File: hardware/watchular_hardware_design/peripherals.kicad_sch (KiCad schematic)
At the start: 45 parts, among them Q1 BSS123, Q2 BSS123, Q3 BSS123, Q4 BSS123

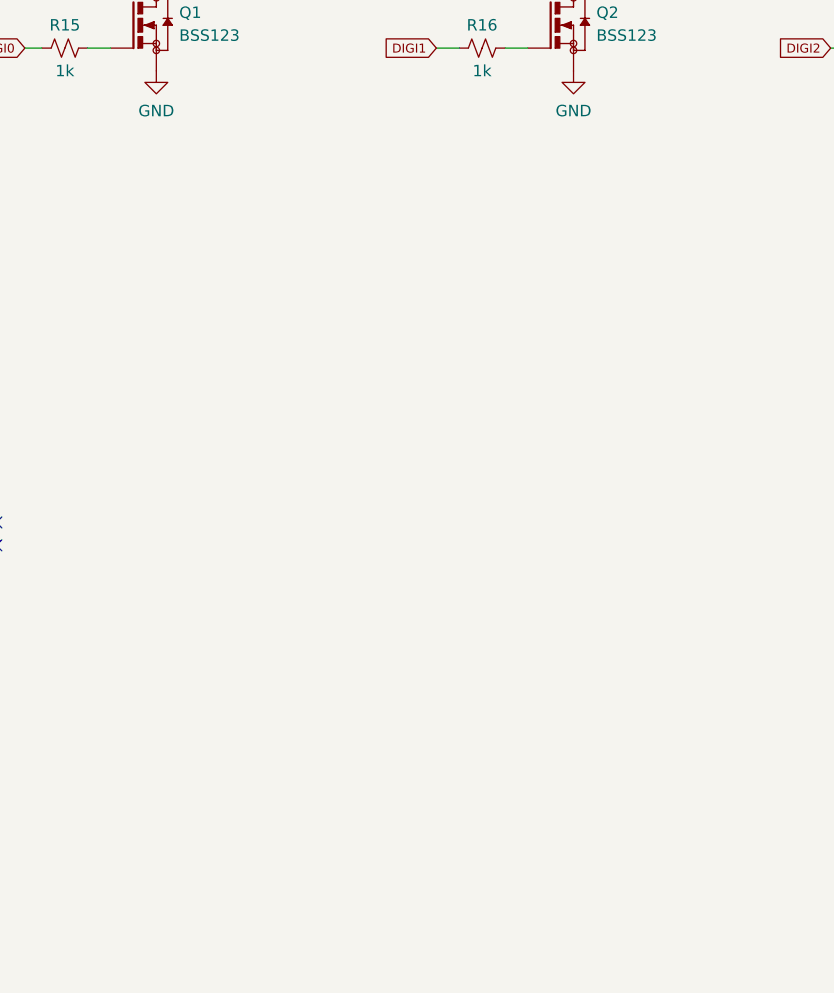
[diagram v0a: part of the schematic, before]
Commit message: Connected MCU pins to the brekout 15 pos header.
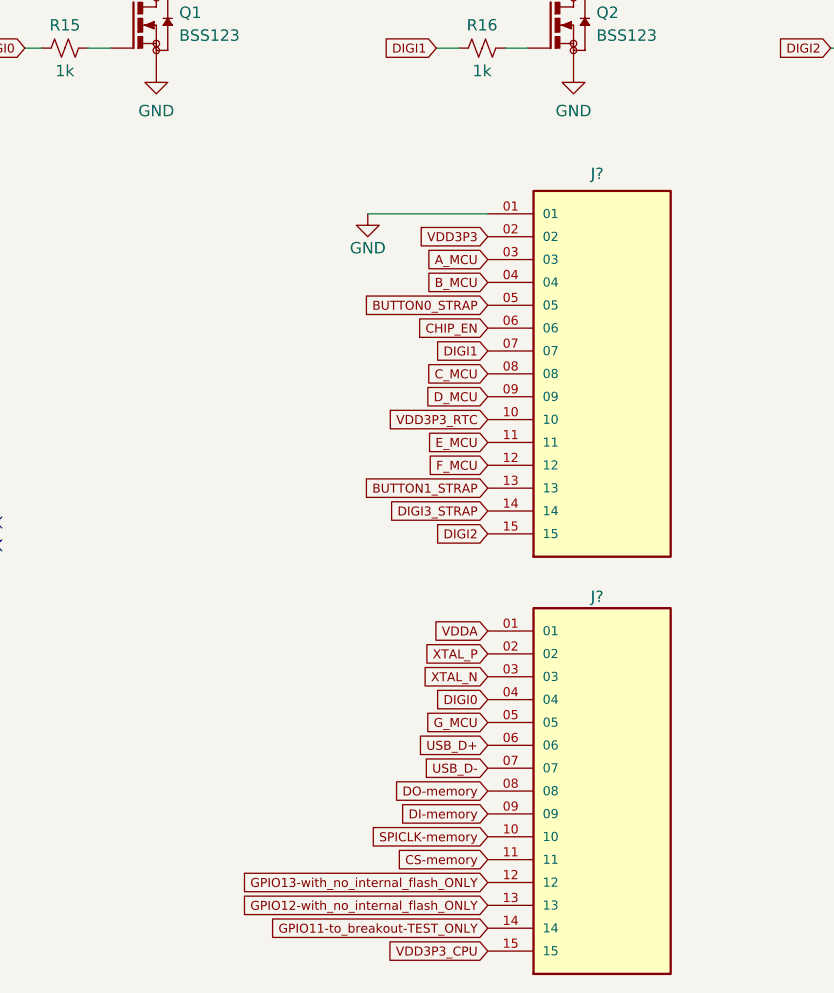
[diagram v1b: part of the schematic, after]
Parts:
- added J? (x2): TSW-115-07-H-S, SAMTEC_TSW-115-07-H-S, symbol TSW-115-07-H-S:TSW-115-07-H-S
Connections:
- net A_MCU: now also J?.03
- net BUTTON0_STRAP: now also J?.05
- net BUTTON1_STRAP: now also J?.13
- net B_MCU: now also J?.04
- net C_MCU: now also J?.08
- net DIGI0: now also J?.04
- net DIGI1: now also J?.07
- net DIGI2: now also J?.15
- net DIGI3_STRAP: now also J?.14
- net D_MCU: now also J?.09
- net E_MCU: now also J?.11
- net F_MCU: now also J?.12
- net GND: now also J?.01
- net G_MCU: now also J?.05
- new net CHIP_EN: J?.06
- new net CS-memory: J?.11
- new net DI-memory: J?.09
- new net DO-memory: J?.08
- new net GPIO11-to_breakout-TEST_ONLY: J?.14
- new net GPIO12-with_no_internal_flash_ONLY: J?.13
- new net GPIO13-with_no_internal_flash_ONLY: J?.12
- new net SPICLK-memory: J?.10
- new net USB_D+: J?.06
- new net USB_D-: J?.07
- new net VDD3P3: J?.02
- new net VDD3P3_CPU: J?.15
- new net VDD3P3_RTC: J?.10
- new net VDDA: J?.01
- new net XTAL_N: J?.03
- new net XTAL_P: J?.02

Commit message: Added battery connector.
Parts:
- added J4: 665102131822, battery_connector-665102131822:665102131822, symbol 665102131822:665102131822
- gave numbers to parts that had none: 2
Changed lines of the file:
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@@
   (symbol (lib_id "power:GND") (at 136.525 88.265 0) (unit 1)
     (in_bom yes) (on_board yes) (fields_autoplaced)
-    (property "Reference" "#PWR032" (id 0) (at 136.525 94.615 0)
+    (property "Reference" "#PWR033" (id 0) (at 136.525 94.615 0)
       (effects (font (size 1.27 1.27)) hide)
     )
@@
   (symbol (lib_id "power:GND") (at 180.34 88.265 0) (unit 1)
     (in_bom yes) (on_board yes) (fields_autoplaced)
-    (property "Reference" "#PWR033" (id 0) (at 180.34 94.615 0)
+    (property "Reference" "#PWR034" (id 0) (at 180.34 94.615 0)
       (effects (font (size 1.27 1.27)) hide)
     )
@@
   (symbol (lib_id "TSW-115-07-H-S:TSW-115-07-H-S") (at 139.7 168.275 0) (unit 1)
     (in_bom yes) (on_board yes)
-    (property "Reference" "J?" (id 0) (at 138.43 146.685 0)
+    (property "Reference" "J3" (id 0) (at 138.43 146.685 0)
       (effects (font (size 1.27 1.27)) (justify left))
     )
@@
   (symbol (lib_id "TSW-115-07-H-S:TSW-115-07-H-S") (at 139.7 121.92 0) (unit 1)
     (in_bom yes) (on_board yes)
-    (property "Reference" "J?" (id 0) (at 138.43 99.695 0)
+    (property "Reference" "J2" (id 0) (at 138.43 99.695 0)
       (effects (font (size 1.27 1.27)) (justify left))
     )
@@
   (symbol (lib_id "power:GND") (at 113.665 104.14 0) (unit 1)
     (in_bom yes) (on_board yes)
-    (property "Reference" "#PWR?" (id 0) (at 113.665 110.49 0)
+    (property "Reference" "#PWR032" (id 0) (at 113.665 110.49 0)
       (effects (font (size 1.27 1.27)) hide)
     )
@@
     (pin "2")
   )
+  (symbol (lib_id "665102131822:665102131822") (at 193.04 121.92 0) (unit 1)
+    (in_bom yes) (on_board yes) (fields_autoplaced)
+    (property "Reference" "J4" (id 0) (at 204.47 121.9199 0)
+      (effects (font (size 1.27 1.27)) (justify left))
+    )
+    (property "Value" "665102131822" (id 1) (at 204.47 124.4599 0)
+      (effects (font (size 1.27 1.27)) (justify left))
+    )
+    (property "Footprint" "battery_connector-665102131822:665102131822" (id 2) (at 193.04 121.92 0)
+      (effects (font (size 1.27 1.27)) (justify left bottom) hide)
+    )
+    (property "Datasheet" "" (id 3) (at 193.04 121.92 0)
+      (effects (font (size 1.27 1.27)) (justify left bottom) hide)
+    )
+    (pin "1")
+    (pin "2")
+  )
   (symbol (lib_id "TL3301AF260QG:TL3301AF260QG") (at 39.37 138.43 0) (unit 1)
     (in_bom yes) (on_board yes) (fields_autoplaced)
@@
   (symbol (lib_id "power:GND") (at 226.695 88.265 0) (unit 1)
     (in_bom yes) (on_board yes) (fields_autoplaced)
-    (property "Reference" "#PWR034" (id 0) (at 226.695 94.615 0)
-      (effects (font (size 1.27 1.27)) hide)
-    )
+    (property "Reference" "#PWR035" (id 0) (at 226.695 94.615 0)
+      (effects (font (size 1.27 1.27)) hide)
+    )

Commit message: Added battery charger.
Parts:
- added U4: MCP73832T-2DCI/OT, battery_charger-MCP73832T:SOT95P280X145-5N, symbol MCP73832T-2DCI_OT:MCP73832T-2DCI/OT
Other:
- moved on the sheet: J4
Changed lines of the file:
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@@
     (pin "2")
   )
-  (symbol (lib_id "665102131822:665102131822") (at 193.04 121.92 0) (unit 1)
+  (symbol (lib_id "665102131822:665102131822") (at 174.625 115.57 0) (unit 1)
     (in_bom yes) (on_board yes) (fields_autoplaced)
-    (property "Reference" "J4" (id 0) (at 204.47 121.9199 0)
+    (property "Reference" "J4" (id 0) (at 186.055 115.5699 0)
       (effects (font (size 1.27 1.27)) (justify left))
     )
-    (property "Value" "665102131822" (id 1) (at 204.47 124.4599 0)
+    (property "Value" "665102131822" (id 1) (at 186.055 118.1099 0)
       (effects (font (size 1.27 1.27)) (justify left))
     )
-    (property "Footprint" "battery_connector-665102131822:665102131822" (id 2) (at 193.04 121.92 0)
+    (property "Footprint" "battery_connector-665102131822:665102131822" (id 2) (at 174.625 115.57 0)
       (effects (font (size 1.27 1.27)) (justify left bottom) hide)
     )
-    (property "Datasheet" "" (id 3) (at 193.04 121.92 0)
+    (property "Datasheet" "" (id 3) (at 174.625 115.57 0)
       (effects (font (size 1.27 1.27)) (justify left bottom) hide)
     )
@@
     (pin "4")
   )
+  (symbol (lib_id "MCP73832T-2DCI_OT:MCP73832T-2DCI{slash}OT") (at 246.38 136.525 0) (unit 1)
+    (in_bom yes) (on_board yes) (fields_autoplaced)
+    (property "Reference" "U4" (id 0) (at 246.38 120.65 0))
+    (property "Value" "MCP73832T-2DCI/OT" (id 1) (at 246.38 123.19 0))
+    (property "Footprint" "battery_charger-MCP73832T:SOT95P280X145-5N" (id 2) (at 246.38 136.525 0)
+      (effects (font (size 1.27 1.27)) (justify left bottom) hide)
+    )
+    (property "Datasheet" "" (id 3) (at 246.38 136.525 0)
+      (effects (font (size 1.27 1.27)) (justify left bottom) hide)
+    )
+    (pin "1")
+    (pin "2")
+    (pin "3")
+    (pin "4")
+    (pin "5")
+  )
   (symbol (lib_id "power:GND") (at 226.695 88.265 0) (unit 1)

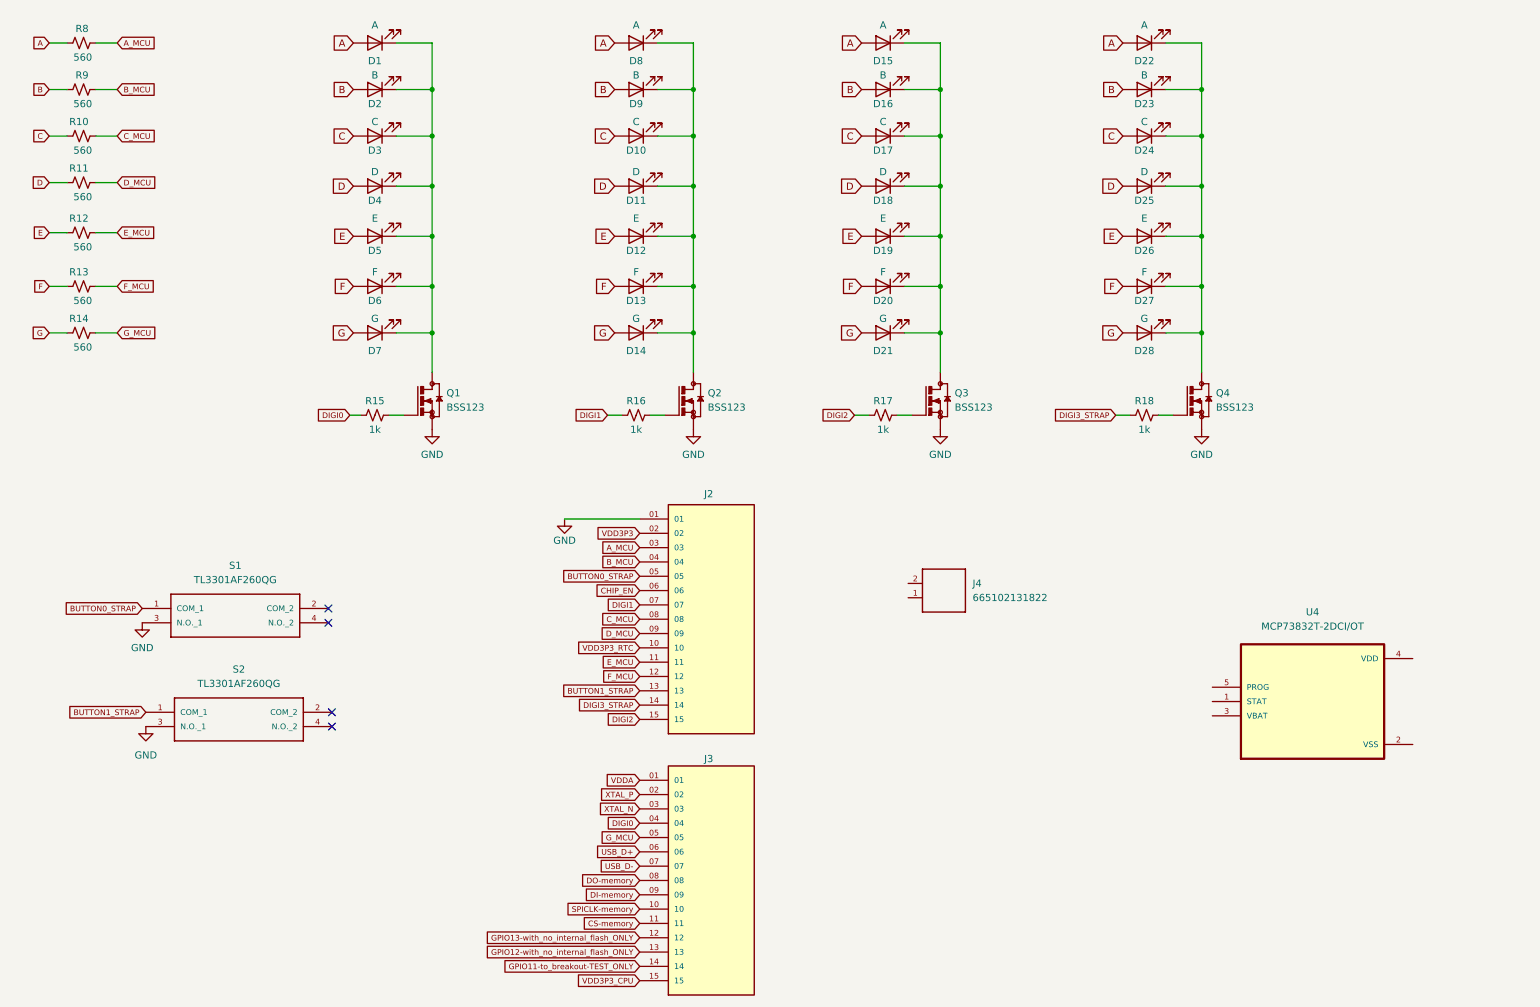
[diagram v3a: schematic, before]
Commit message: Added mosfet for controlling the power source.
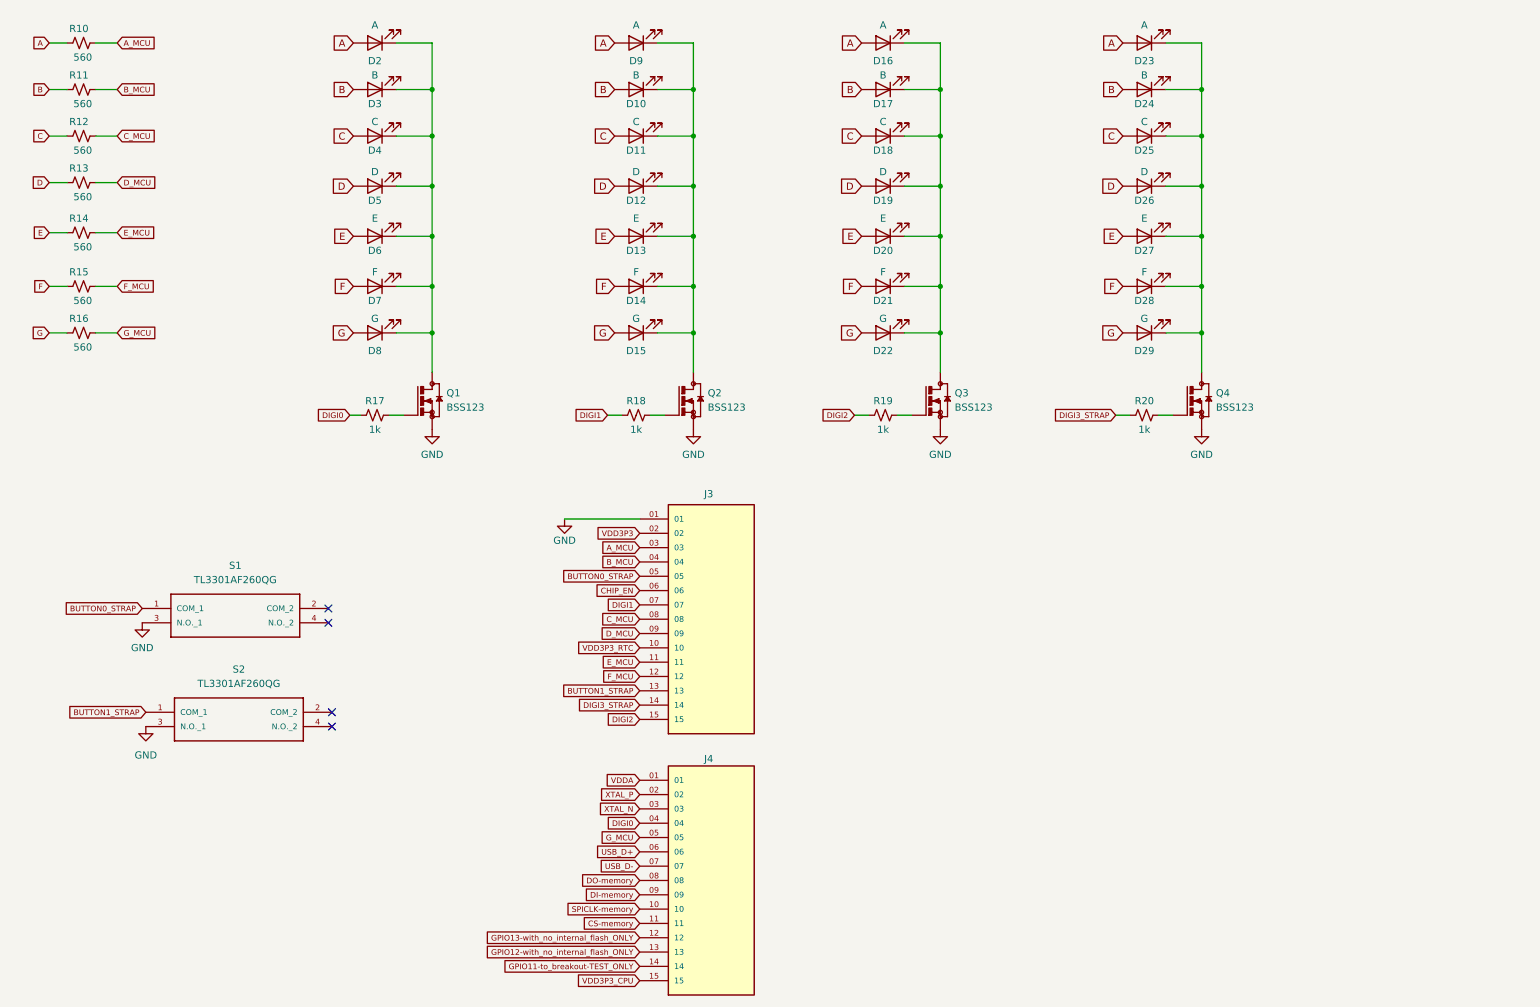
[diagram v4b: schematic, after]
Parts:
- removed J4: 665102131822, battery_connector-665102131822:665102131822, symbol 665102131822:665102131822
- removed U4: MCP73832T-2DCI/OT, battery_charger-MCP73832T:SOT95P280X145-5N, symbol MCP73832T-2DCI_OT:MCP73832T-2DCI/OT
- renumbered D9 to D10, D10 to D11, D11 to D12, D12 to D13, D13 to D14, D14 to D15, D15 to D16, D16 to D17, D17 to D18, D18 to D19, D1 to D2, D19 to D20, D20 to D21, D21 to D22, D22 to D23, D23 to D24, D24 to D25, D25 to D26, D26 to D27, D27 to D28, D28 to D29, D2 to D3, D3 to D4, D4 to D5, D5 to D6, D6 to D7, D7 to D8, D8 to D9, J2 to J3, J3 to J4, R8 to R10, R9 to R11, R10 to R12, R11 to R13, R12 to R14, R13 to R15, R14 to R16, R15 to R17, R16 to R18, R17 to R19, R18 to R20

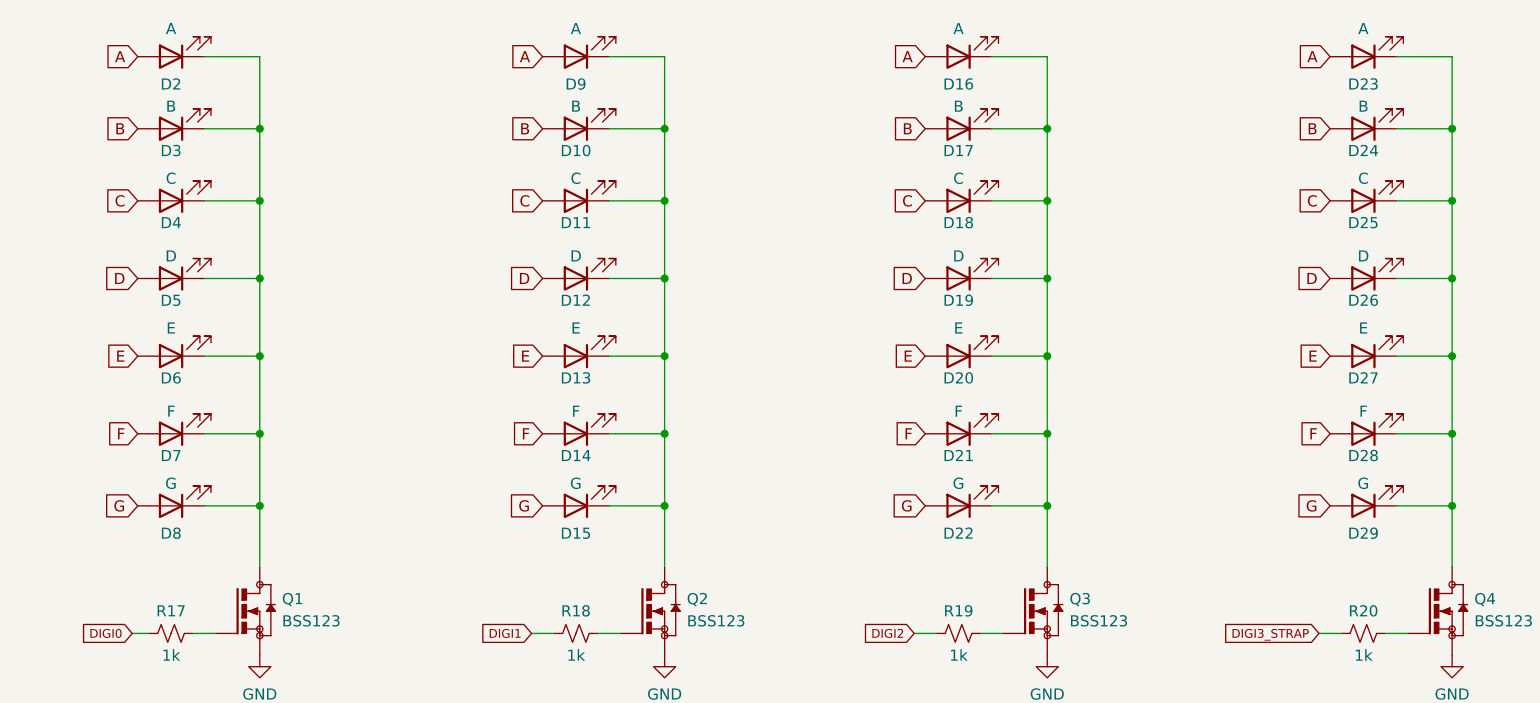
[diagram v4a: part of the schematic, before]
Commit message: Added schottky diode.
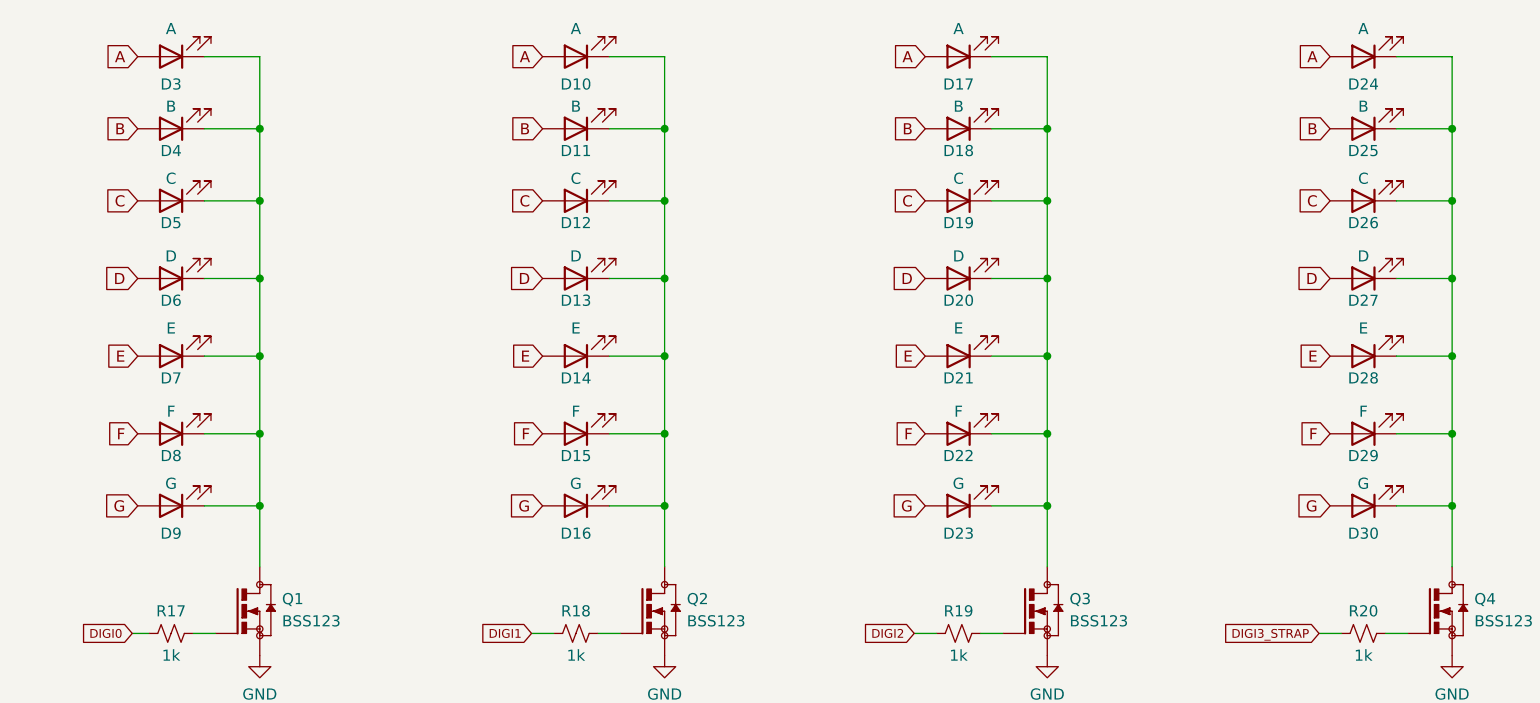
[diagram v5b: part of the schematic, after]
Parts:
- J3, J4: footprint SAMTEC_TSW-115-07-H-S -> header-TSW-115-07-H-S:SAMTEC_TSW-115-07-H-S
- renumbered D9 to D10, D10 to D11, D11 to D12, D12 to D13, D13 to D14, D14 to D15, D15 to D16, D16 to D17, D17 to D18, D18 to D19, D19 to D20, D20 to D21, D21 to D22, D22 to D23, D23 to D24, D24 to D25, D25 to D26, D26 to D27, D27 to D28, D28 to D29, D2 to D3, D29 to D30, D3 to D4, D4 to D5, D5 to D6, D6 to D7, D7 to D8, D8 to D9
